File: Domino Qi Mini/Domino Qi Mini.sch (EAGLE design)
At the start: 90 parts, among them J1 MH22-1, J2 MH22-1, M1 DOMINO, Q1 AP2302GN, Q2 2SC4081, SW1 IT-1210, SW2 IT-1210, SW3 IT-1210, U1 MP65151DJ, U2 ATMEGA32U4-AU/MU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

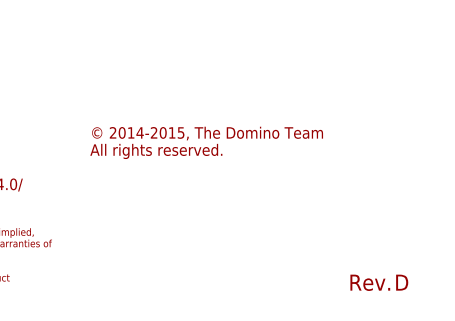
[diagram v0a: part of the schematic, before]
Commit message: Changed Domino Qi Mini to 4 layers
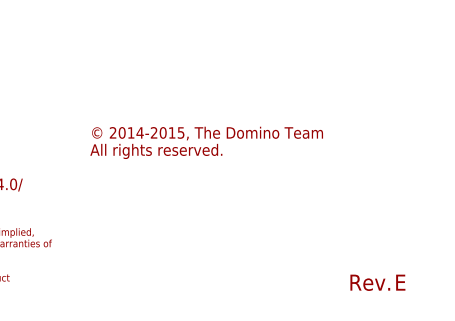
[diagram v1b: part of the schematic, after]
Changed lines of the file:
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@@
 <attribute name="DATABASE" value="./../Common/BOM/Domino_DB.txt"/>
 <attribute name="DRAWN" value="M.STEMPIN"/>
-<attribute name="REV" value="D"/>
+<attribute name="REV" value="E"/>
 </attributes>
 <variantdefs>
@@
 <class number="0" name="default" width="0" drill="0">
 </class>
-<class number="1" name="USB" width="0.3683" drill="0">
+<class number="1" name="USB" width="0.2794" drill="0">
 <clearance class="0" value="0.1524"/>
 <clearance class="1" value="0.1524"/>
 </class>
-<class number="2" name="RF" width="0.6604" drill="0">
+<class number="2" name="RF" width="0.3556" drill="0">
 <clearance class="2" value="0.1524"/>
 </class>
-<class number="3" name="Ethernet" width="0.254" drill="0">
+<class number="3" name="Ethernet" width="0.2032" drill="0">
 <clearance class="0" value="0.1524"/>
 <clearance class="1" value="0.1524"/>
@@
 </segment>
 </net>
-<net name="A2" class="0">
+<net name="A2" class="3">
 <segment>
 <pinref part="U2" gate="G$1" pin="(ADC5/TMS)PF5"/>
@@
 </segment>
 </net>
-<net name="P4_TX-" class="0">
+<net name="P4_TX-" class="3">
 <segment>
 <wire x1="271.78" y1="45.72" x2="271.78" y2="55.88" width="0.1524" layer="91"/>
@@
 </segment>
 </net>
-<net name="P4_TX+" class="0">
+<net name="P4_TX+" class="3">
 <segment>
 <wire x1="269.24" y1="55.88" x2="269.24" y2="45.72" width="0.1524" layer="91"/>
@@
 </segment>
 </net>
-<net name="P4_RX-" class="0">
+<net name="P4_RX-" class="3">
 <segment>
 <wire x1="266.7" y1="45.72" x2="266.7" y2="55.88" width="0.1524" layer="91"/>
@@
 </segment>
 </net>
-<net name="P4_RX+" class="0">
+<net name="P4_RX+" class="3">
 <segment>
 <wire x1="264.16" y1="55.88" x2="264.16" y2="45.72" width="0.1524" layer="91"/>
